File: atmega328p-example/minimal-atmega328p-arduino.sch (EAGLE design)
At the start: 27 parts, among them J1 3x2 M, J2 1x6 M, J4 POWER_JACK, U1 NCP1117ST50T3G, U4 ATMEGA328P-PU, Y1 16 MHz

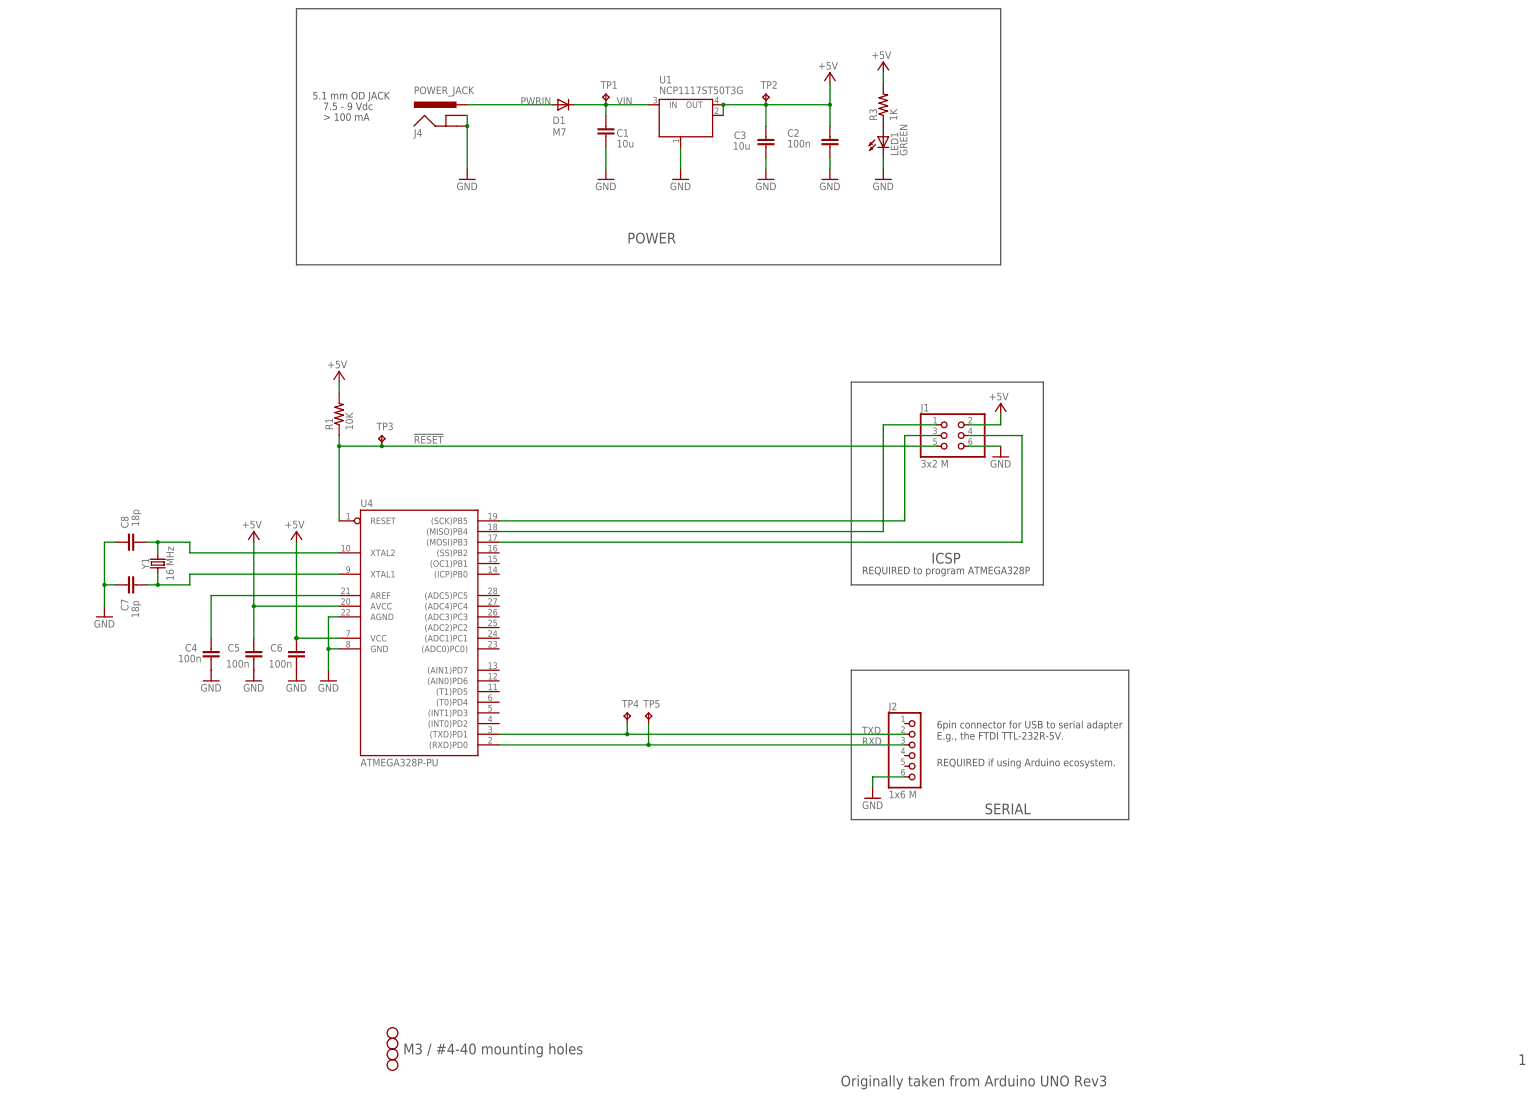
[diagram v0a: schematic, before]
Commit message: Added microusb connector for power with DNP zero ohms, updated BOM.
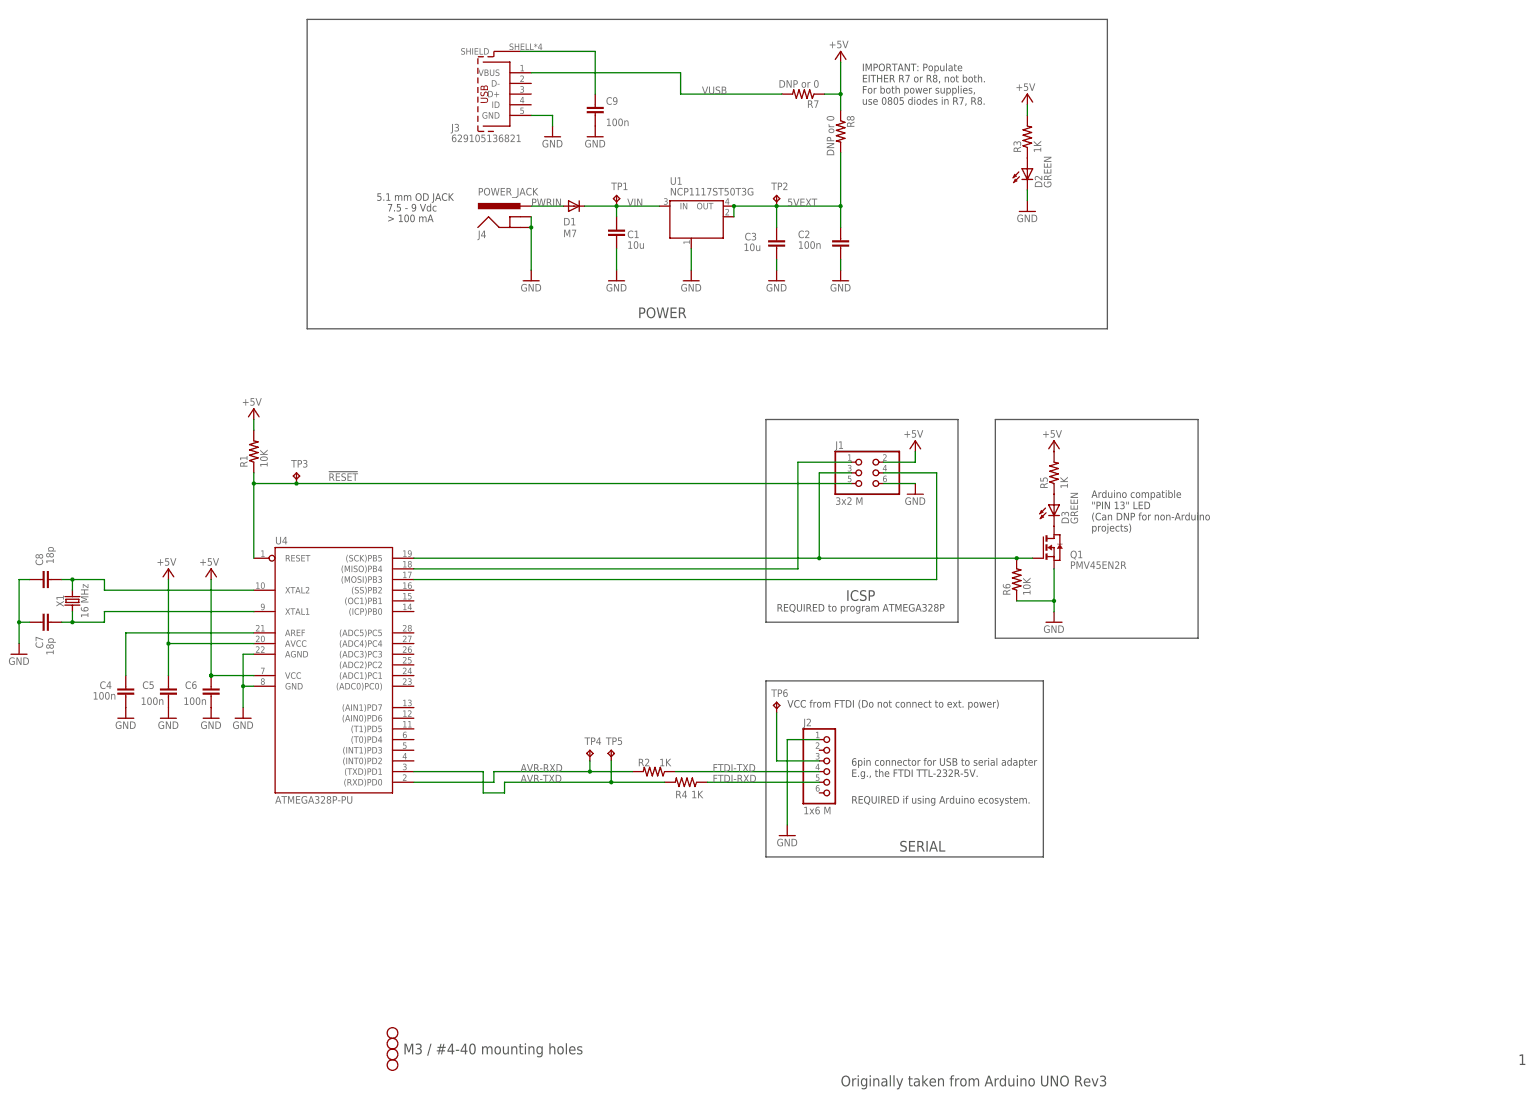
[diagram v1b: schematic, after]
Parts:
- removed LED1: GREEN, led:LEDCHIP-LED0805
- removed Y1: 16 MHz, SparkFun-Clocks:CRYSTALSMD-HC49UP
- added C9: 100n, rcl:C-EUC0805K
- added D2, D3: GREEN, led:LEDCHIP-LED0805
- added J3: 629105136821, Wurth_Elektronik_Electromechanic_Input-Output_Connectors_rev19b:629105136821
- added Q1: PMV45EN2R, zetex:NMOSSOT23
- added R2, R4, R5: 1K, rcl:R-US_R0805
- added R6: 10K, rcl:R-US_R0805
- added R7, R8: DNP or 0, rcl:R-US_R0805
- added TP6: TPPAD1-13, testpad:TPPAD1-13
- added X1: 16 MHz, SparkFun-Clocks:CRYSTALSMD-HC49UP
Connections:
- removed net RXD: J2.3, TP5.TP, U4.(RXD)PD0
- removed net TXD: J2.2, TP4.TP, U4.(TXD)PD1
- new net 5VEXT: C2.2, C3.1, R8.2, TP2.TP, U1.OUT, U1.OUT@1
- new net AVR-RXD: R2.2, TP4.TP, U4.(RXD)PD0
- new net AVR-TXD: R4.2, TP5.TP, U4.(TXD)PD1
- new net FTDI-RXD: J2.5, R4.1
- new net FTDI-TXD: J2.4, R2.1
- new net N$2: D3.A, R5.1
- new net N$4: D3.C, Q1.D
- new net N$5: J2.3, TP6.TP
- new net N$6: C9.2, J3.SHIELD
- new net VUSB: J3.VBUS, R7.2
- net +5V: now also R5.2, R7.1, R8.1; no longer C2.2, C3.1, TP2.TP, U1.OUT, U1.OUT@1
- net GND: now also C9.1, D2.C, J2.1, J3.GND, Q1.S, R6.1; no longer J2.6, LED1.C
- net N$3: now also D2.A; no longer LED1.A
- net SCK: now also Q1.G, R6.2
- net XTAL1: now also X1.1; no longer Y1.1
- net XTAL2: now also X1.2; no longer Y1.2
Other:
- note added: "Arduino compatible "PIN 13" LED (Can DNP for non-Arduino projects)"
- note added: "IMPORTANT: Populate EITHER R7 or R8, not both. For both power supplies, use 0805 diodes in R7, R8."
- note added: "VCC from FTDI (Do not connect to ext. power)"
- moved on the sheet: C1, C2, C3, C4, C5, C6, C7, C8, D1, J1, J2, J4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

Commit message: Added reset switch, moved programming wires to bottom layer.
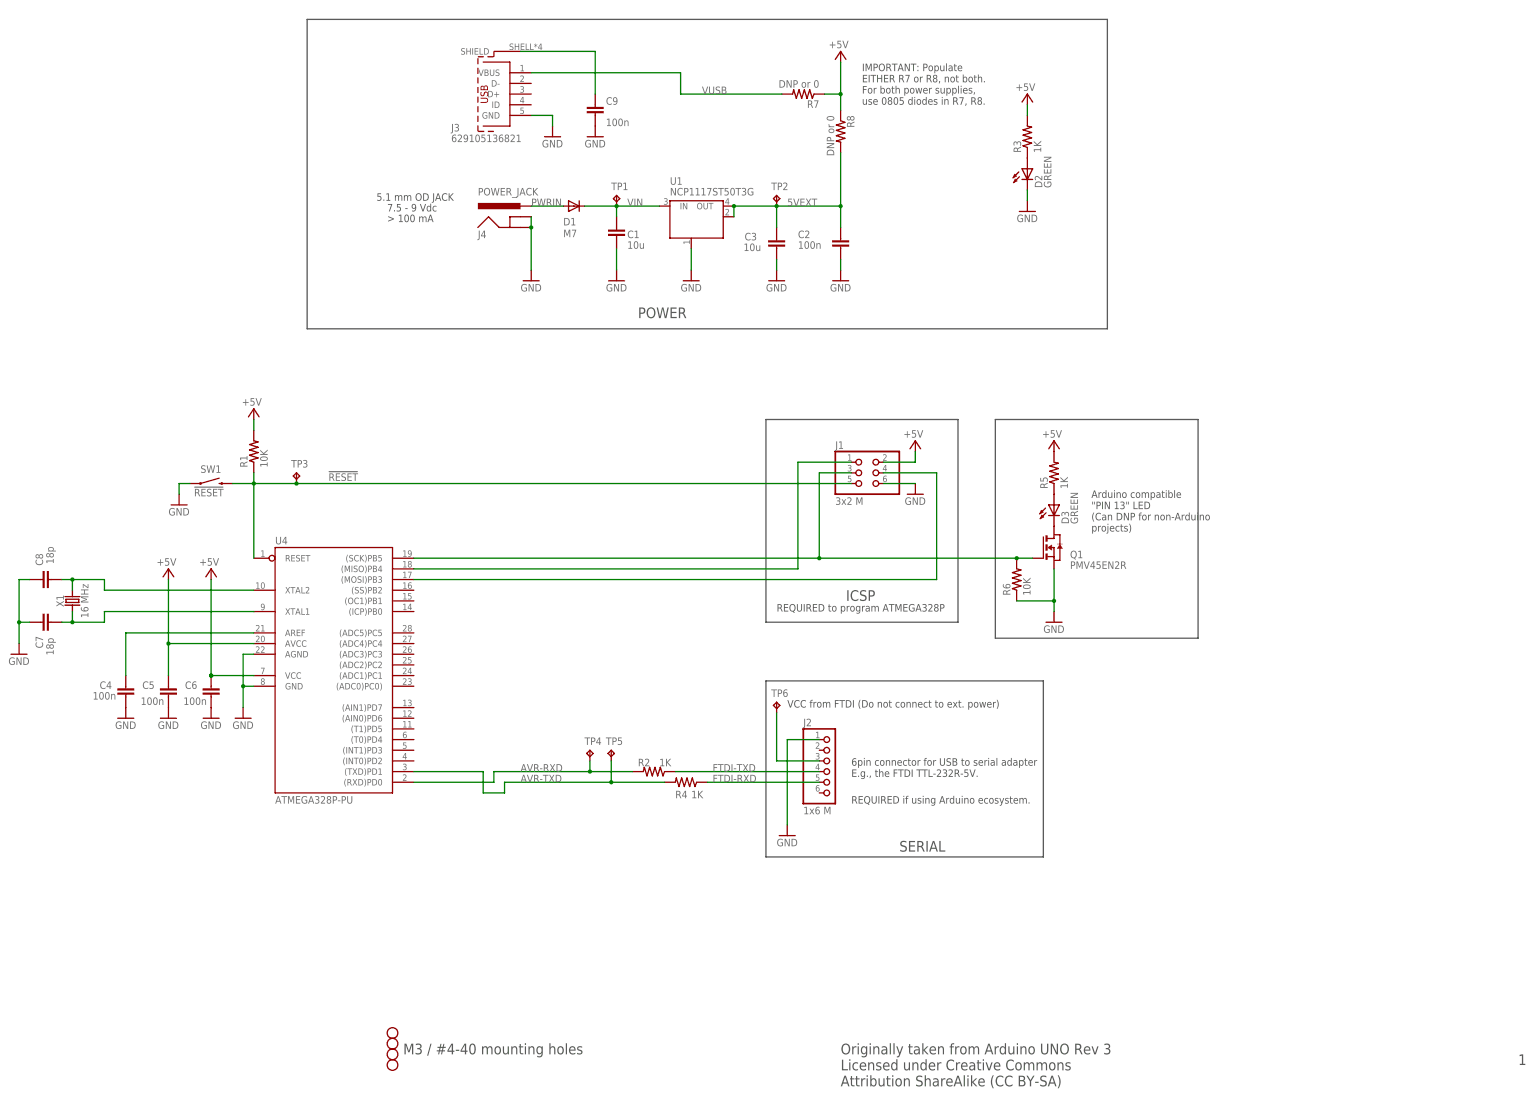
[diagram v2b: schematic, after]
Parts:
- added SW1: !RESET, SparkFun-Electromechanical:SWITCH-MOMENTARY-2SMD
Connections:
- net !RESET: now also SW1.2
- net GND: now also SW1.1
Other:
- note added: "Originally taken from Arduino UNO Rev 3 Licensed under Creative Commons Attribution ShareAlike (CC BY-SA)"
- note removed: "Originally taken from Arduino UNO Rev3"
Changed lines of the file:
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@@
 <attribute name="MPN" value="629105136821"/>
 </part>
+<part name="SW1" library="SparkFun-Electromechanical" deviceset="SWITCH-MOMENTARY-2" device="SMD" value="!RESET">
+<attribute name="DESC" value="SWITCH TACTILE SPST-NO 0.05A 12V"/>
+<attribute name="MFR" value="C&amp;K"/>
+<attribute name="MPN" value="RS-187R05A2-DS MT RT"/>
+</part>
+<part name="GND16" library="supply1" deviceset="GND" device=""/>
 </parts>
 <sheets>
 <sheet>
 <plain>
-<text x="256.54" y="2.54" size="2.54" layer="97">Originally taken from Arduino UNO Rev3</text>
 <text x="148.59" y="210.82" size="1.778" layer="97">7.5 - 9 Vdc</text>
 <text x="208.28" y="185.42" size="2.54" layer="97">POWER</text>
@@
 For both power supplies,
 use 0805 diodes in R7, R8.</text>
+<text x="256.54" y="2.54" size="2.54" layer="97">Originally taken from Arduino UNO Rev 3
+Licensed under Creative Commons
+Attribution ShareAlike (CC BY-SA)</text>
 </plain>
 <instances>
@@
 <attribute name="MPN" x="175.26" y="238.76" size="1.778" layer="96" rot="R180" display="off"/>
 </instance>
+<instance part="SW1" gate="G$1" x="106.68" y="146.05" smashed="yes">
+<attribute name="NAME" x="104.14" y="148.59" size="1.778" layer="95"/>
+<attribute name="VALUE" x="102.616" y="143.002" size="1.778" layer="96"/>
+<attribute name="DESC" x="106.68" y="146.05" size="1.778" layer="96" display="off"/>
+<attribute name="MFR" x="106.68" y="146.05" size="1.778" layer="96" display="off"/>
+<attribute name="MPN" x="106.68" y="146.05" size="1.778" layer="96" display="off"/>
+</instance>
+<instance part="GND16" gate="1" x="99.06" y="140.97" smashed="yes">
+<attribute name="VALUE" x="96.52" y="138.43" size="1.778" layer="96"/>
+</instance>
 </instances>
 <busses>
@@
 <pinref part="C9" gate="G$1" pin="1"/>
 <pinref part="GND15" gate="1" pin="GND"/>
+</segment>
+<segment>
+<pinref part="GND16" gate="1" pin="GND"/>
+<wire x1="99.06" y1="143.51" x2="99.06" y2="146.05" width="0.1524" layer="91"/>
+<pinref part="SW1" gate="G$1" pin="1"/>
+<wire x1="99.06" y1="146.05" x2="101.6" y2="146.05" width="0.1524" layer="91"/>
 </segment>
 </net>
@@
 <wire x1="127" y1="146.05" x2="116.84" y2="146.05" width="0.1524" layer="91"/>
 <junction x="127" y="146.05"/>
+<pinref part="SW1" gate="G$1" pin="2"/>
+<wire x1="111.76" y1="146.05" x2="116.84" y2="146.05" width="0.1524" layer="91"/>
 </segment>
 </net>
